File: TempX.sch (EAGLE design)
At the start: 6 parts, among them U1 TMP36

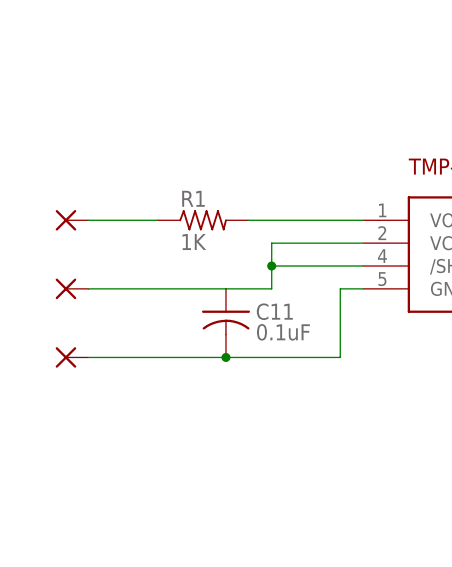
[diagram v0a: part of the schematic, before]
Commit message: changed design to circular
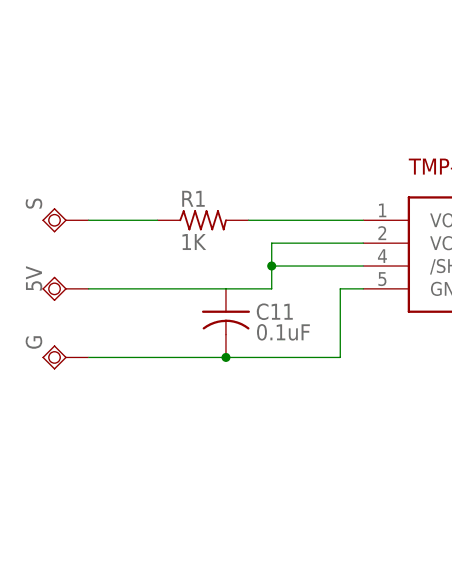
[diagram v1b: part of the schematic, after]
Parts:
- removed GND, OUT: WIREPAD3,17/1,2, wirepad:WIREPAD3,17/1,2
- added G, S: TPSQTP20R, testpad:TPSQTP20R
- 5V: value WIREPAD3,17/1,2 -> TPSQTP20R; device wirepad:WIREPAD3,17/1,2 -> testpad:TPSQTP20R
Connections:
- net 5V: now also 5V.TP; no longer 5V.P
- net C1: now also G.TP; no longer GND.P
- net N$1: now also S.TP; no longer OUT.P

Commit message: change layout to rectangle
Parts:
- 5V, G, S: value TPSQTP20R -> TPSQPAD1-17; device testpad:TPSQTP20R -> testpad:TPSQPAD1-17
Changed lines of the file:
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@@
 <part name="R1" library="rcl" deviceset="R-US_" device="R0603" value="1K"/>
 <part name="C11" library="rcl" deviceset="C-US" device="C0603" value="0.1uF"/>
-<part name="S" library="testpad" deviceset="TPSQ" device="TP20R" value="TPSQTP20R"/>
-<part name="5V" library="testpad" deviceset="TPSQ" device="TP20R" value="TPSQTP20R"/>
-<part name="G" library="testpad" deviceset="TPSQ" device="TP20R" value="TPSQTP20R"/>
+<part name="S" library="testpad" deviceset="TPSQ" device="PAD1-17" value="TPSQPAD1-17"/>
+<part name="5V" library="testpad" deviceset="TPSQ" device="PAD1-17" value="TPSQPAD1-17"/>
+<part name="G" library="testpad" deviceset="TPSQ" device="PAD1-17" value="TPSQPAD1-17"/>
 </parts>
 <sheets>
